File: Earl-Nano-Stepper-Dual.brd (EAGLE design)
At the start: 99.8 x 68.8 mm, 29 parts, among them IC1 ULN2003AN, J4 CONNECTOR-M03254-LOCK, M1 ARDUINO-NANO-3.0, SW1 PB1, SW2 PB2, SW3 Toggle 1

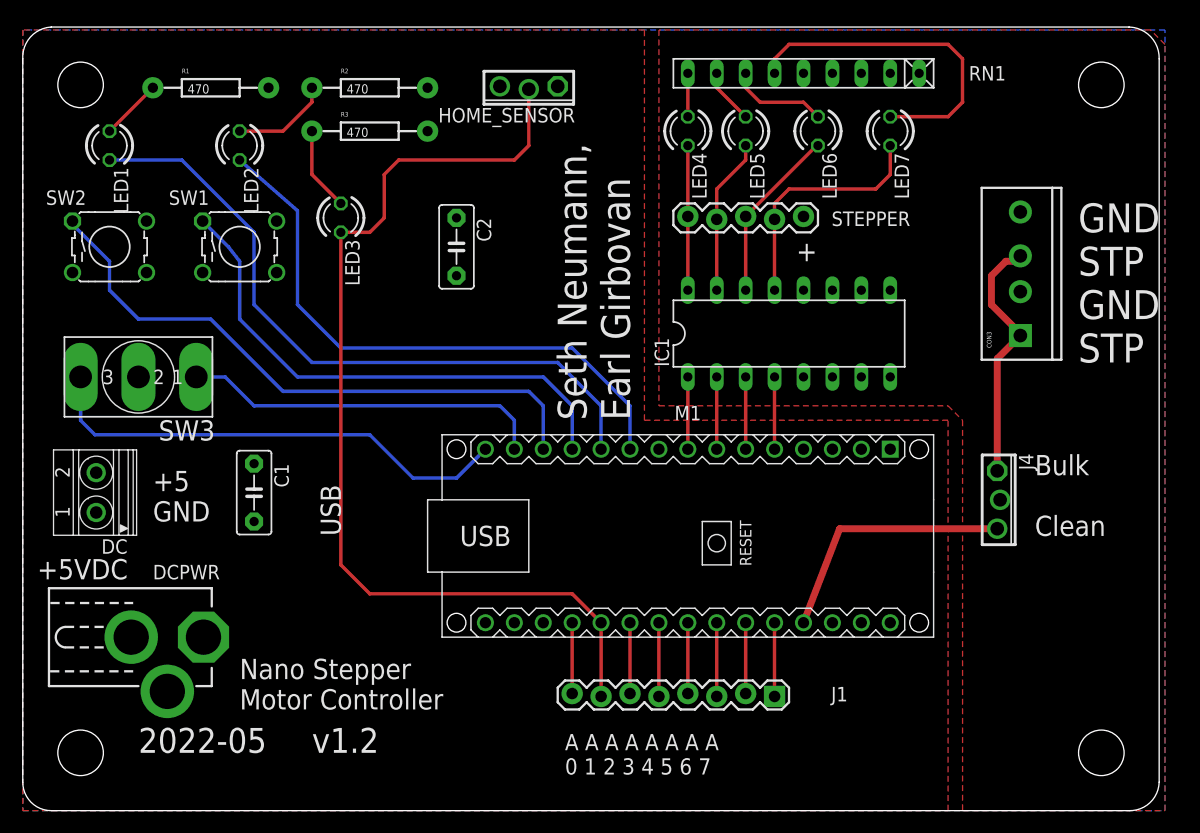
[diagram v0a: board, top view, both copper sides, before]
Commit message: changes to support two stepper motors
changed to ULN2803
Moved both home sensors to A6,A7
Added LEDs, 2nd connector etc
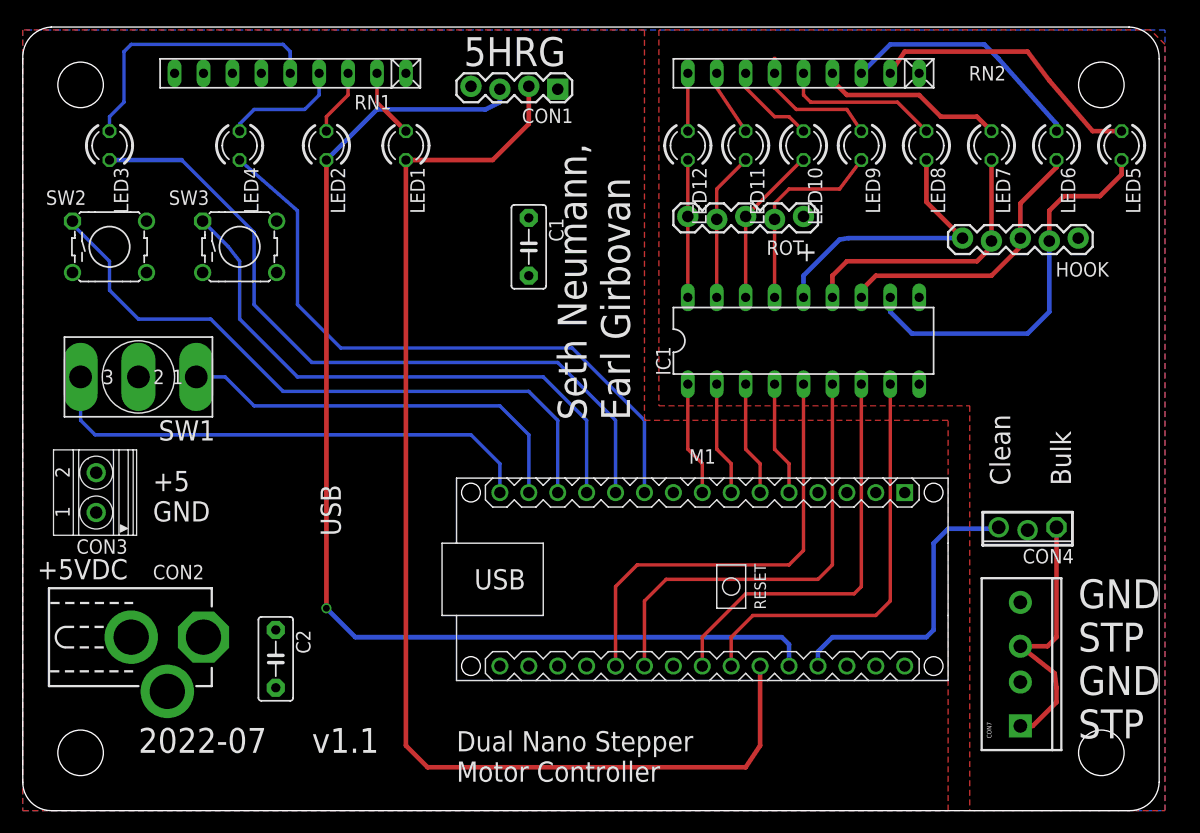
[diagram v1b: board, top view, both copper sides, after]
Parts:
- removed DC: (no value), SPCoast:1751248
- removed HOME_SENSOR, J4: CONNECTOR-M03254-LOCK, SPCoast:3POL254
- removed J1: (no value), SPCoast:1X08_LOCK
- removed R1, R2, R3: 470, SPCoast:AXIAL-0.4-RES
- added CON1: (no value), SPCoast:1X04_LOCK
- added CON4: CONNECTOR-M03254-LOCK, SPCoast:3POL254
- added CON7: (no value), SPCoast:SCREWTERMINAL-3.5MM-4_LOCK
- added HOOK: B5B-XH, SPCoast:1X05_LOCK
- added LED10, LED11, LED12, LED8, LED9: RED, SPCoast:LED3MM
- added RN2: 1000, resistor-net:RN-9
- C1: value .1uF -> 10uF
- C2: value 10uF -> .1uF
- CON3: device SPCoast:SCREWTERMINAL-3.5MM-4_LOCK -> SPCoast:1751248
- IC1: value ULN2003AN -> ULN2803; device uln-udn:DIL16 -> uln-udn:DIL18
- LED1, LED2: value RED -> GRN
- LED3: value GRN -> RED
- RN1: value (none) -> 1000
- SW1: value PB1 -> Toggle 1; device SPCoast:4P-PTH-6.0X6.0X5.0H -> SPCoast:SWITCH-SPDT-508
- SW3: value Toggle 1 -> PB1; device SPCoast:SWITCH-SPDT-508 -> SPCoast:4P-PTH-6.0X6.0X5.0H
- moved CON3 82.5 mm to (6.35, 27.9)
- moved RN1 45.1 mm to (23.5, 64.8)
- moved C2 39.5 mm to (22.2, 13.3)
- moved LED4 39.4 mm to (19.1, 58.4)
- moved LED5 33.0 mm to (96.5, 58.4)
- moved C1 32.4 mm to (44.5, 49.5)
- moved LED1 26.0 mm to (33.7, 58.4)
- moved LED3 21.3 mm to (7.62, 58.4)
- moved LED6 21.0 mm to (90.8, 58.4)
- moved U$3 20.5 mm to (69.8, 2.54)
- moved SW1 14.5 mm to (10.2, 38.1), turned to 180 degrees
- moved SW3 14.5 mm to (19.1, 49.5), turned to 0 degrees
- moved LED7 8.98 mm to (85.1, 58.4)
- moved LED2 7.62 mm to (26.7, 58.4)
- moved M1 4.02 mm to (59.7, 20.3)
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- renumbered DCPWR to CON2, STEPPER to ROT
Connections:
- removed net A1: HOME_SENSOR.2, J1.7, LED3.K, M1.J2.11
- new net N$28: CON4.1, CON7.1, CON7.3
- new net N$31: LED6.A, RN2.3
- new net N$32: HOOK.1, IC1.14, LED8.K
- new net N$33: HOOK.2, IC1.13, LED7.K
- new net N$34: HOOK.3, IC1.12, LED6.K
- new net N$35: HOOK.4, IC1.11, LED5.K
- new net N$36: LED7.A, RN2.4
- new net N$37: LED8.A, RN2.5
- net +5V: now also CON1.4, CON3.2, CON4.3, RN1.1; no longer DC.2, HOME_SENSOR.3, J4.3, R1.P$2, R2.P$2, R3.P$2
- net GND: now also CON1.1, CON3.1, CON7.2, CON7.4, IC1.9, SW1.2, SW3.3; no longer CON3.2, CON3.4, DC.1, HOME_SENSOR.1, IC1.8, SW1.3, SW3.2
- net N$1: now also IC1.18, LED12.K; no longer IC1.16, LED4.K
- net N$10: now also LED2.A, RN1.3; no longer LED3.A, R3.P$1
- net N$15: now also IC1.17, LED11.K; no longer IC1.15, LED5.K
- net N$16: now also IC1.16, LED10.K; no longer IC1.14, LED6.K
- net N$17: now also IC1.15, LED9.K; no longer IC1.13, LED7.K
- net N$18: now also LED9.A, RN2.6; no longer LED7.A, RN1.6
- net N$19: now also CON1.3, LED2.K, M1.J2.5; no longer CON3.1, CON3.3, J4.1
- net N$2: now also SW1.3; no longer SW3.3
- net N$20: now also LED10.A, RN2.7; no longer LED6.A, RN1.7
- net N$21: now also LED11.A, RN2.8; no longer LED5.A, RN1.8
- net N$22: now also LED12.A, RN2.9; no longer LED4.A, RN1.9
- net N$23: now also IC1.5, M1.J2.11; no longer J1.8, M1.J2.12
- net N$24: now also IC1.6; no longer J1.6
- net N$25: now also IC1.7, M1.J2.8; no longer J1.5, M1.J2.9
- net N$26: now also IC1.8, M1.J2.7; no longer J1.4, M1.J2.8
- net N$27: now also LED5.A, RN2.2; no longer J1.3, M1.J2.7
- net N$29: now also CON1.2, LED1.K; no longer J1.2
- net N$3: now also SW1.1; no longer SW3.1
- net N$30: now also LED1.A, RN1.2; no longer J1.1, M1.J2.5
- net N$5: now also SW3.1; no longer SW1.1
- net N$6: now also LED3.K; no longer LED1.K
- net N$7: now also LED4.K; no longer LED2.K
- net N$8: now also LED3.A, RN1.5; no longer LED1.A, R1.P$1
- net N$9: now also LED4.A, RN1.4; no longer LED2.A, R2.P$1
- net STP_PWR: now also CON4.2, HOOK.5, IC1.10, RN2.1; no longer IC1.9, J4.2, RN1.1
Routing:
- net N$29: track 6.35 -> 106.8 mm
- net A1: track 87.4 -> 0.00 mm
- net N$19: track 22.3 -> 101.6 mm, vias 0 -> 1
- net N$35: track 0.00 -> 34.6 mm
- net N$23: track 6.35 -> 40.1 mm
- net N$24: track 6.35 -> 39.4 mm
- net N$26: track 6.35 -> 36.9 mm
- net N$25: track 6.35 -> 36.1 mm
- net N$32: track 0.00 -> 25.4 mm
- net N$34: track 0.00 -> 25.1 mm
- net N$33: track 0.00 -> 24.5 mm
- net N$28: track 0.00 -> 23.6 mm
- net N$31: track 0.00 -> 21.9 mm
- net N$8: track 5.39 -> 24.5 mm
- net N$27: track 6.35 -> 24.7 mm
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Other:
- board text added: "2022-07"
- board text added: "5HRG"
- board text added: "Clean Bulk"
- board text added: "Dual Nano Stepper Motor Controller"
- board text added: "v1.1"
- board text removed: "2022-05"
- board text removed: "A A A A A A A A 0 1 2 3 4 5 6 7"
- board text removed: "Bulk Clean"
- board text removed: "Nano Stepper Motor Controller"
- board text removed: "v1.2"

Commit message: changes resulting initial board order
changes resulting in initial board order
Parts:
- renumbered CON1 to HOME, HOOK to S1, ROT to S2
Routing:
- net GND: track 0.00 -> 2.17 mm
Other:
- board text added: "512G"
- board text removed: "5HRG"
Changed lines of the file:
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@@
 <text x="92.075" y="28.575" size="1.778" layer="21" font="vector" ratio="10" rot="R90">Clean
 Bulk</text>
-<text x="38.735" y="65.405" size="2.54" layer="21" font="vector" ratio="10">5HRG</text>
+<text x="38.735" y="65.405" size="2.54" layer="21" font="vector" ratio="10">512G</text>
 </plain>
 <attributes>
@@
 <element name="C1" library="capacitor-wima" package="C5B3" value="10uF" x="44.45" y="49.53" rot="R270"/>
 <element name="U$3" library="MRCSLogoTop" package="MRCSLOGOTOP" value="" x="69.85" y="2.54"/>
-<element name="ROT" library="SPCoast" package="1X05_LOCK" value="B5B-XH" x="58.42" y="52.07" smashed="yes">
+<element name="S2" library="SPCoast" package="1X05_LOCK" value="B5B-XH" x="58.42" y="52.07" smashed="yes">
 <attribute name="NAME" x="65.3288" y="48.8188" size="1.27" layer="25" ratio="10"/>
-<attribute name="VALUE" x="57.15" y="48.895" size="1.27" layer="27"/>
 </element>
 <element name="CON4" library="SPCoast" package="3POL254" value="CONNECTOR-M03254-LOCK" x="88.265" y="24.765" smashed="yes" rot="R180">
@@
 <element name="U$4" library="MRCSLogoBtm" package="MRCSLOGOBTM" value="" x="25.4" y="20.32"/>
 <element name="IC1" library="uln-udn" package="DIL18" value="ULN2803" x="68.58" y="41.275"/>
-<element name="CON1" library="SPCoast" package="1X04_LOCK" value="" x="46.99" y="63.5" rot="R180"/>
+<element name="HOME" library="SPCoast" package="1X04_LOCK" value="" x="46.99" y="63.5" smashed="yes" rot="R180">
+<attribute name="NAME" x="53.4162" y="67.3862" size="1.27" layer="25" ratio="10" rot="R180"/>
+<attribute name="VALUE" x="48.26" y="66.675" size="1.27" layer="27" rot="R180"/>
+</element>
 <element name="LED1" library="SPCoast" package="LED3MM" value="GRN" x="33.655" y="58.42" rot="R90"/>
-<element name="HOOK" library="SPCoast" package="1X05_LOCK" value="B5B-XH" x="82.55" y="50.165" smashed="yes">
+<element name="S1" library="SPCoast" package="1X05_LOCK" value="B5B-XH" x="82.55" y="50.165" smashed="yes">
 <attribute name="NAME" x="90.7288" y="46.9138" size="1.27" layer="25" ratio="10"/>
-<attribute name="VALUE" x="81.28" y="46.99" size="1.27" layer="27"/>
 </element>
 <element name="LED8" library="SPCoast" package="LED3MM" value="RED" x="79.375" y="58.42" rot="R90"/>
@@
 <contactref element="CON7" pad="4"/>
 <contactref element="CON7" pad="2"/>
-<contactref element="CON1" pad="1"/>
+<contactref element="HOME" pad="1"/>
 <contactref element="M1" pad="J1.4"/>
 <contactref element="C2" pad="2"/>
+<wire x1="74.93" y1="12.7" x2="74.93" y2="11.43" width="0.4064" layer="1"/>
+<wire x1="86.995" y1="10.795" x2="87.63" y2="11.43" width="0.4064" layer="1"/>
+<wire x1="87.63" y1="11.2978" x2="87.63" y2="11.43" width="0" layer="19" extent="1-1"/>
 </signal>
 <signal name="N$2">
@@
 </polygon>
 <contactref element="M1" pad="J2.4"/>
-<contactref element="CON1" pad="4"/>
+<contactref element="HOME" pad="4"/>
 <contactref element="RN1" pad="1"/>
 <contactref element="C2" pad="1"/>
@@
 </signal>
 <signal name="N$1">
-<contactref element="ROT" pad="1"/>
+<contactref element="S2" pad="1"/>
 <contactref element="LED12" pad="K"/>
 <wire x1="58.42" y1="57.15" x2="58.42" y2="52.197" width="0.3048" layer="1"/>
@@
 </signal>
 <signal name="N$15">
-<contactref element="ROT" pad="2"/>
+<contactref element="S2" pad="2"/>
 <contactref element="LED11" pad="K"/>
 <wire x1="63.5" y1="57.15" x2="60.96" y2="54.61" width="0.3048" layer="1"/>
@@
 </signal>
 <signal name="N$16">
-<contactref element="ROT" pad="3"/>
+<contactref element="S2" pad="3"/>
 <contactref element="LED10" pad="K"/>
 <wire x1="68.58" y1="57.15" x2="68.453" y2="57.15" width="0.3048" layer="1"/>
@@
 </signal>
 <signal name="N$17">
-<contactref element="ROT" pad="4"/>
+<contactref element="S2" pad="4"/>
 <contactref element="LED9" pad="K"/>
 <wire x1="66.04" y1="51.943" x2="66.04" y2="53.34" width="0.3048" layer="1"/>
@@
 <contactref element="IC1" pad="10"/>
 <contactref element="CON4" pad="2"/>
-<contactref element="HOOK" pad="5"/>
-<contactref element="ROT" pad="5"/>
+<contactref element="S1" pad="5"/>
+<contactref element="S2" pad="5"/>
 </signal>
 <signal name="N$13">
@@
 <signal name="N$29">
 <contactref element="M1" pad="J2.6"/>
-<contactref element="CON1" pad="2"/>
+<contactref element="HOME" pad="2"/>
 <contactref element="LED1" pad="K"/>
 <wire x1="44.45" y1="63.627" x2="44.45" y2="60.325" width="0.4064" layer="1"/>
@@
 <signal name="N$19">
 <contactref element="LED2" pad="K"/>
-<contactref element="CON1" pad="3"/>
+<contactref element="HOME" pad="3"/>
 <contactref element="M1" pad="J2.5"/>
 <wire x1="41.91" y1="63.373" x2="41.91" y2="62.23" width="0.4064" layer="16"/>
@@
 <signal name="N$32">
 <contactref element="IC1" pad="14"/>
-<contactref element="HOOK" pad="1"/>
+<contactref element="S1" pad="1"/>
 <contactref element="LED8" pad="K"/>
 <wire x1="79.375" y1="57.15" x2="79.375" y2="53.467" width="0.4064" layer="1"/>
@@
 <signal name="N$33">
 <contactref element="IC1" pad="13"/>
-<contactref element="HOOK" pad="2"/>
+<contactref element="S1" pad="2"/>
 <contactref element="LED7" pad="K"/>
 <wire x1="85.09" y1="57.15" x2="85.09" y2="50.038" width="0.4064" layer="1"/>
@@
 <signal name="N$34">
 <contactref element="IC1" pad="12"/>
-<contactref element="HOOK" pad="3"/>
+<contactref element="S1" pad="3"/>
 <contactref element="LED6" pad="K"/>
 <wire x1="90.805" y1="57.15" x2="90.805" y2="56.515" width="0.4064" layer="1"/>
@@
 <signal name="N$35">
 <contactref element="IC1" pad="11"/>
-<contactref element="HOOK" pad="4"/>
+<contactref element="S1" pad="4"/>
 <contactref element="LED5" pad="K"/>
 <wire x1="96.52" y1="57.15" x2="96.52" y2="55.88" width="0.4064" layer="1"/>
